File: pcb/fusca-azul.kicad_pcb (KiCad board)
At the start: 2 copper layers, 6 parts, among them J1 L298N Logic Jumpers, J2 HC-SR04, U1 ESP32-DEVKIT-V1

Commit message: feat: atualiza a pcb, mas falta corrigir tamanho e organização
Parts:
- removed J1: L298N Logic Jumpers, Connector_PinSocket_2.54mm:PinSocket_1x06_P2.54mm_Vertical
- removed J2: HC-SR04, Connector_PinSocket_2.54mm:PinSocket_1x04_P2.54mm_Vertical
- removed R1: 2k, Resistor_THT:R_Axial_DIN0207_L6.3mm_D2.5mm_P2.54mm_Vertical
- removed R2: 1k, Resistor_THT:R_Axial_DIN0207_L6.3mm_D2.5mm_P2.54mm_Vertical
- removed U1: ESP32-DEVKIT-V1, RF_Module:ESP32-C3-DevKitM-1
- added J3: HC-SR04, Connector_PinSocket_2.54mm:PinSocket_1x04_P2.54mm_Vertical, F.Cu at (150.7, 86.8)
- added J4: L298N Logic Jumpers, Connector_PinSocket_2.54mm:PinSocket_1x06_P2.54mm_Vertical, F.Cu at (112.0, 99.6)
- added J5: HC-SR04, Connector_PinSocket_2.54mm:PinSocket_1x04_P2.54mm_Vertical, F.Cu at (134.3, 60.6)
- added J6: HC-SR04, Connector_PinSocket_2.54mm:PinSocket_1x04_P2.54mm_Vertical, F.Cu at (107.7, 79.2)
- added R3: 2k, Resistor_THT:R_Axial_DIN0207_L6.3mm_D2.5mm_P2.54mm_Vertical, F.Cu at (145.3, 78.9)
- added R4: 1k, Resistor_THT:R_Axial_DIN0207_L6.3mm_D2.5mm_P2.54mm_Vertical, F.Cu at (145.3, 82.0)
- added R5: 2k, Resistor_THT:R_Axial_DIN0207_L6.3mm_D2.5mm_P2.54mm_Vertical, F.Cu at (126.1, 64.1)
- added R6: 1k, Resistor_THT:R_Axial_DIN0207_L6.3mm_D2.5mm_P2.54mm_Vertical, F.Cu at (129.3, 66.2)
- added R7: 2k, Resistor_THT:R_Axial_DIN0207_L6.3mm_D2.5mm_P2.54mm_Vertical, F.Cu at (111.2, 78.8)
- added R8: 1k, Resistor_THT:R_Axial_DIN0207_L6.3mm_D2.5mm_P2.54mm_Vertical, F.Cu at (113.6, 83.2)
- added U2: ESP32 - HW-394, fusca-azul:ESP32-HW-394, F.Cu at (118.8, 75.4)
- 5V_IN1: footprint TerminalBlock_Phoenix:TerminalBlock_Phoenix_PT-1,5-2-3.5-H_1x02_P3.50mm_Horizontal -> TerminalBlock_Phoenix:TerminalBlock_Phoenix_MKDS-1,5-2-5.08_1x02_P5.08mm_Horizontal
- moved 5V_IN1 47.3 mm to (108.1, 104.6)
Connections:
- 5V_IN1 pad 1: +5V -> GND
- 5V_IN1 pad 2: GND -> +5V
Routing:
- net GND: track 0.00 -> 167.8 mm, vias 0 -> 4
- net +5V: track 0.00 -> 143.8 mm
- net Net-(U2-D34): track 0.00 -> 29.7 mm
- net Net-(J5-Trig): track 0.00 -> 26.7 mm
- net Net-(J1-IN_3): track 19.9 -> 0.00 mm
- net Net-(J6-Trig): track 0.00 -> 16.2 mm
- net Net-(U2-D35): track 0.00 -> 11.6 mm
- net Net-(J3-Trig): track 0.00 -> 9.54 mm
- net Net-(J4-ENA): track 0.00 -> 9.40 mm
- net Net-(J4-IN_1): track 0.00 -> 8.35 mm
- net Net-(J4-IN_4): track 0.00 -> 8.35 mm
- net Net-(J4-IN_3): track 0.00 -> 8.35 mm
- net Net-(J4-IN_2): track 0.00 -> 8.35 mm
- net Net-(J4-ENB): track 0.00 -> 8.35 mm
- net Net-(J1-IN_2): track 7.50 -> 0.00 mm
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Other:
- board outline added: 56.5 x 65.2 mm

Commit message: feat: finaliza pcb
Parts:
- moved J5 55.1 mm to (86.5, 88.0), turned to 0 degrees
- moved J3 49.1 mm to (107.4, 110.0), turned to 90 degrees
- moved R6 44.6 mm to (91.5, 90.0), turned to -90 degrees
- moved R5 40.1 mm to (95.5, 90.0)
- moved 5V_IN1 38.0 mm to (87.0, 72.9)
- moved J6 32.2 mm to (135.5, 95.5), turned to 180 degrees
- moved J4 31.6 mm to (130.0, 73.7)
- moved U2 24.6 mm to (98.9, 60.9)
- moved R8 22.9 mm to (112.5, 106.0), turned to 90 degrees
- moved R7 21.2 mm to (112.5, 100.0)
- moved R4 15.4 mm to (130.0, 84.0)
- moved R3 15.4 mm to (130.0, 80.5)
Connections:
- J3 pad 2: Net-(J3-Trig) -> unconnected-(J3-Trig-Pad2)
- R3 pad 1: Net-(U2-D22) -> Net-(U2-RX2)
- R4 pad 1: Net-(U2-D22) -> Net-(U2-RX2)
- R4 pad 2: Net-(J3-Echo) -> Net-(J6-Echo)
- R5 pad 1: GND -> Net-(U2-D25)
- R5 pad 2: Net-(U2-D34) -> GND
- R6 pad 1: Net-(U2-D34) -> Net-(U2-D25)
- R7 pad 1: Net-(U2-D35) -> Net-(R7-Pad1)
- R8 pad 1: Net-(U2-D35) -> Net-(J3-Echo)
- R8 pad 2: Net-(J6-Echo) -> Net-(R7-Pad1)
- U2 pad 10: Net-(J6-Trig) -> unconnected-(U2-D32-Pad10)
- U2 pad 11: Net-(U2-D35) -> unconnected-(U2-D35-Pad11)
- U2 pad 12: Net-(U2-D34) -> unconnected-(U2-D34-Pad12)
- U2 pad 18: unconnected-(U2-D15-Pad18) -> Net-(J6-Trig)
- U2 pad 21: unconnected-(U2-RX2-Pad21) -> Net-(U2-RX2)
- U2 pad 22: unconnected-(U2-TX2-Pad22) -> Net-(J4-ENA)
- U2 pad 24: unconnected-(U2-D18-Pad24) -> Net-(J4-IN_1)
- U2 pad 25: unconnected-(U2-D19-Pad25) -> Net-(J4-IN_2)
- U2 pad 26: Net-(J3-Trig) -> Net-(J4-IN_3)
- U2 pad 29: Net-(U2-D22) -> Net-(J4-IN_4)
- U2 pad 3: Net-(J4-ENA) -> unconnected-(U2-D13-Pad3)
- U2 pad 30: Net-(J5-Trig) -> Net-(J4-ENB)
- U2 pad 5: Net-(J4-IN_1) -> unconnected-(U2-D14-Pad5)
- U2 pad 6: Net-(J4-IN_2) -> unconnected-(U2-D27-Pad6)
- U2 pad 7: Net-(J4-IN_3) -> unconnected-(U2-D26-Pad7)
- U2 pad 8: Net-(J4-IN_4) -> Net-(U2-D25)
- U2 pad 9: Net-(J4-ENB) -> Net-(J5-Trig)
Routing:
- net +5V: track 143.8 -> 96.8 mm
- net unconnected-(J3-Trig-Pad2): track 0.00 -> 30.8 mm
- net Net-(U2-D34): track 29.7 -> 0.00 mm
- net Net-(R7-Pad1): track 0.00 -> 27.9 mm
- net Net-(U2-D25): track 0.00 -> 16.8 mm
- net GND: track 167.8 -> 151.0 mm, vias 4 -> 2
- net Net-(U2-D35): track 11.6 -> 0.00 mm
- net Net-(J3-Trig): track 9.54 -> 0.00 mm
- net Net-(U2-RX2): track 0.00 -> 9.24 mm
- net Net-(J5-Trig): track 26.7 -> 19.5 mm
- net Net-(U2-D22): track 7.08 -> 0.00 mm
- net Net-(J6-Trig): track 16.2 -> 11.8 mm
- net Net-(J6-Echo): track 3.84 -> 7.66 mm
- net Net-(J4-IN_4): track 8.35 -> 5.71 mm
- net Net-(J4-ENB): track 8.35 -> 5.71 mm
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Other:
- board size 56.5 x 65.2 mm -> 59 x 67.5 mm

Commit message: fix: corrige ligacao na placa
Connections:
- J3 pad 2: unconnected-(J3-Trig-Pad2) -> Net-(J3-Trig)
- R7 pad 1: Net-(R7-Pad1) -> Net-(U2-D26)
- R8 pad 2: Net-(R7-Pad1) -> Net-(U2-D26)
- U2 pad 6: unconnected-(U2-D27-Pad6) -> Net-(J3-Trig)
- U2 pad 7: unconnected-(U2-D26-Pad7) -> Net-(U2-D26)
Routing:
- net unconnected-(J3-Trig-Pad2): track 30.8 -> 0.00 mm
- net Net-(J3-Trig): track 0.00 -> 30.8 mm
- net GND: track 151.0 -> 179.1 mm, vias 2 -> 0
- net Net-(U2-D26): track 0.00 -> 27.9 mm
- net Net-(R7-Pad1): track 27.9 -> 0.00 mm
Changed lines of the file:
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@@
 			(at 0 -2.77 0)
 			(layer "F.SilkS")
+			(hide yes)
 			(effects
 				(font
@@
 			(at 0 -2.77 0)
 			(layer "F.SilkS")
+			(hide yes)
 			(effects
 				(font
@@
 			(at 1.27 -2.37 90)
 			(layer "F.SilkS")
+			(hide yes)
 			(effects
 				(font
@@
 			(at 0 -2.77 0)
 			(layer "F.SilkS")
+			(hide yes)
 			(effects
 				(font
@@
 			(at 0 -2.77 90)
 			(layer "F.SilkS")
+			(hide yes)
 			(effects
 				(font
@@
 			(layers "*.Cu" "*.Mask")
 			(remove_unused_layers no)
-			(net "unconnected-(J3-Trig-Pad2)")
+			(net "Net-(J3-Trig)")
 			(pinfunction "Trig_2")
 			(pintype "input")
@@
 			(keep_end_layers yes)
 			(zone_layer_connections)
-			(net "unconnected-(U2-D27-Pad6)")
+			(net "Net-(J3-Trig)")
 			(pinfunction "D27_6")
 			(pintype "bidirectional")
@@
 			(keep_end_layers yes)
 			(zone_layer_connections)
-			(net "unconnected-(U2-D26-Pad7)")
+			(net "Net-(U2-D26)")
 			(pinfunction "D26_7")
 			(pintype "bidirectional")
@@
 			(at 1.27 -2.37 90)
 			(layer "F.SilkS")
+			(hide yes)
 			(effects
 				(font
@@
 			(at 1.27 -2.37 0)
 			(layer "F.SilkS")
+			(hide yes)
 			(effects
 				(font
@@
 			(at 1.27 -2.37 0)
 			(layer "F.SilkS")
+			(hide yes)
 			(effects
 				(font
@@
 			(layers "*.Cu" "*.Mask")
 			(remove_unused_layers no)
-			(net "Net-(R7-Pad1)")
+			(net "Net-(U2-D26)")
 			(pintype "passive")
 		)
@@
 			(at 1.27 -2.37 90)
 			(layer "F.SilkS")
+			(hide yes)
 			(effects
 				(font
@@
 			(layers "*.Cu" "*.Mask")
 			(remove_unused_layers no)
-			(net "Net-(R7-Pad1)")
+			(net "Net-(U2-D26)")
 			(pintype "passive")
 		)
@@
 			(at 1.27 -2.37 0)
 			(layer "F.SilkS")
+			(hide yes)
 			(effects
 				(font
@@
 	)
 	(segment
-		(start 115.04 110)
-		(end 115.04 100.04)
+		(start 121 51)
+		(end 121 97)
 		(width 1)
 		(layer "F.Cu")
@@
 	)
 	(segment
-		(start 129.605 93.895)
-		(end 130 93.5)
+		(start 115.04 110)
+		(end 115.04 100.04)
 		(width 1)
 		(layer "F.Cu")
@@
 	)
 	(segment
-		(start 124.325 93.895)
-		(end 129.605 93.895)
+		(start 92.46 95.58)
+		(end 95.5 92.54)
 		(width 1)
 		(layer "F.Cu")
@@
 	)
 	(segment
-		(start 92.46 95.58)
-		(end 95.5 92.54)
+		(start 121 51)
+		(end 122 51)
 		(width 1)
 		(layer "F.Cu")
@@
 	)
 	(segment
-		(start 118.22 100)
+		(start 121.11 97.11)
 		(end 122.11 96.11)
 		(width 1)
@@
 	(segment
 		(start 98.5 51)
-		(end 122 51)
+		(end 121 51)
 		(width 1)
 		(layer "F.Cu")
@@
 	)
 	(segment
+		(start 118.22 100)
+		(end 121.11 97.11)
+		(width 1)
+		(layer "F.Cu")
+		(net "GND")
+	)
+	(segment
 		(start 95.5 54)
 		(end 98.5 51)
@@
 		(net "GND")
 	)
-	(via
-		(at 135.5 83.505)
-		(size 0.6)
-		(drill 0.3)
-		(layers "F.Cu" "B.Cu")
-		(net "GND")
-	)
-	(via
-		(at 130 93.5)
-		(size 0.6)
-		(drill 0.3)
-		(layers "F.Cu" "B.Cu")
-		(net "GND")
-	)
 	(segment
-		(start 130 93.5)
-		(end 130 89.005)
+		(start 121 97)
+		(end 121.11 97.11)
 		(width 1)
-		(layer "B.Cu")
-		(net "GND")
-	)
-	(segment
-		(start 130 89.005)
-		(end 135.5 83.505)
-		(width 1)
-		(layer "B.Cu")
+		(layer "F.Cu")
 		(net "GND")
 	)
@@
 		(width 0.5)
 		(layer "F.Cu")
-		(net "unconnected-(J3-Trig-Pad2)")
+		(net "Net-(J3-Trig)")
 	)
 	(segment
@@
 		(width 0.5)
 		(layer "F.Cu")
-		(net "unconnected-(J3-Trig-Pad2)")
+		(net "Net-(J3-Trig)")
 	)
 	(segment
@@
 		(width 0.5)
 		(layer "F.Cu")
-		(net "Net-(R7-Pad1)")
+		(net "Net-(U2-D26)")
 	)
 	(segment
@@
 		(width 0.5)
 		(layer "F.Cu")
-		(net "Net-(R7-Pad1)")
+		(net "Net-(U2-D26)")
 	)
 	(segment
@@
 		(width 0.5)
 		(layer "F.Cu")
-		(net "Net-(R7-Pad1)")
+		(net "Net-(U2-D26)")
 	)
 	(segment
@@
 		(width 0.5)
 		(layer "F.Cu")
-		(net "Net-(R7-Pad1)")
+		(net "Net-(U2-D26)")
 	)
 	(embedded_fonts no)

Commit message: finaliza pcb
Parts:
- removed J6: HC-SR04, Connector_PinSocket_2.54mm:PinSocket_1x04_P2.54mm_Vertical
- removed R3: 2k, Resistor_THT:R_Axial_DIN0207_L6.3mm_D2.5mm_P2.54mm_Vertical
- removed R4: 1k, Resistor_THT:R_Axial_DIN0207_L6.3mm_D2.5mm_P2.54mm_Vertical
- R5, R6, R7, R8: footprint Resistor_THT:R_Axial_DIN0207_L6.3mm_D2.5mm_P2.54mm_Vertical -> Resistor_THT:R_Axial_DIN0207_L6.3mm_D2.5mm_P5.08mm_Vertical
- moved 5V_IN1 83.3 mm to (154.0, 122.4), turned to 90 degrees
- moved R5 37.2 mm to (111.6, 123.5)
- moved U2 34.2 mm to (119.7, 88.0)
- moved R6 33.6 mm to (106.7, 119.9), turned to 0 degrees
- moved J5 32.3 mm to (102.8, 115.9)
- moved J4 30.2 mm to (152.3, 94.0), turned to 0 degrees
- moved J3 27.9 mm to (102.9, 82.5), turned to 0 degrees
- moved R8 18.9 mm to (107.7, 87.8), turned to 0 degrees
- moved R7 9.53 mm to (107.8, 91.7)
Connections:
- R5 pad 1: Net-(U2-D25) -> Net-(U2-D14)
- R6 pad 1: Net-(U2-D25) -> Net-(J5-Echo)
- R6 pad 2: Net-(J5-Echo) -> Net-(U2-D14)
- R7 pad 1: Net-(U2-D26) -> GND
- R7 pad 2: GND -> Net-(U2-D26)
- U2 pad 18: Net-(J6-Trig) -> unconnected-(U2-D15-Pad18)
- U2 pad 20: unconnected-(U2-D4-Pad20) -> Net-(J4-ENB)
- U2 pad 21: Net-(U2-RX2) -> unconnected-(U2-RX2-Pad21)
- U2 pad 22: Net-(J4-ENA) -> unconnected-(U2-TX2-Pad22)
- U2 pad 24: Net-(J4-IN_1) -> Net-(J4-IN_4)
- U2 pad 25: Net-(J4-IN_2) -> Net-(J4-IN_3)
- U2 pad 26: Net-(J4-IN_3) -> Net-(J4-IN_2)
- U2 pad 29: Net-(J4-IN_4) -> Net-(J4-IN_1)
- U2 pad 30: Net-(J4-ENB) -> Net-(J4-ENA)
- U2 pad 5: unconnected-(U2-D14-Pad5) -> Net-(U2-D14)
- U2 pad 6: Net-(J3-Trig) -> Net-(J5-Trig)
- U2 pad 8: Net-(U2-D25) -> unconnected-(U2-D25-Pad8)
- U2 pad 9: Net-(J5-Trig) -> Net-(J3-Trig)
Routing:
- net GND: track 179.1 -> 131.0 mm
- net +5V: track 96.8 -> 143.8 mm
- net Net-(U2-D25): track 16.8 -> 0.00 mm
- net Net-(U2-D14): track 0.00 -> 14.3 mm
- net Net-(J6-Trig): track 11.8 -> 0.00 mm
- net Net-(U2-RX2): track 9.24 -> 0.00 mm
- net Net-(J6-Echo): track 7.66 -> 0.00 mm
- net Net-(U2-D26): track 27.9 -> 23.4 mm
- net Net-(J4-ENB): track 5.71 -> 9.96 mm
- net Net-(J4-IN_1): track 7.74 -> 9.65 mm
- net Net-(J4-IN_4): track 5.71 -> 7.55 mm
- net Net-(J3-Trig): track 30.8 -> 32.7 mm
- net Net-(J3-Echo): track 3.96 -> 4.88 mm
- net Net-(J5-Echo): track 5.23 -> 4.32 mm
- net Net-(J5-Trig): track 19.5 -> 20.1 mm
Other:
- board size 59 x 67.5 mm -> 64.6 x 55.3 mm

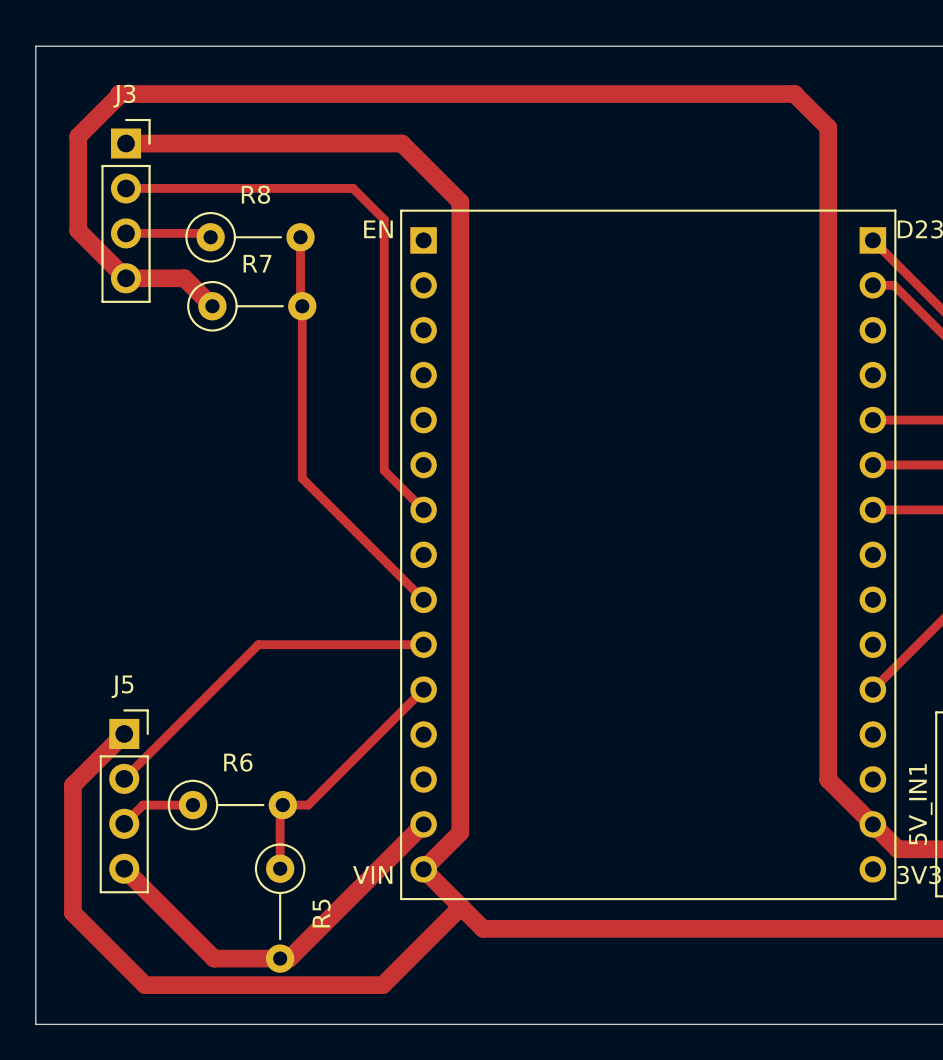
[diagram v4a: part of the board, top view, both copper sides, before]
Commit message: corrige pcb com espaçamento erraado
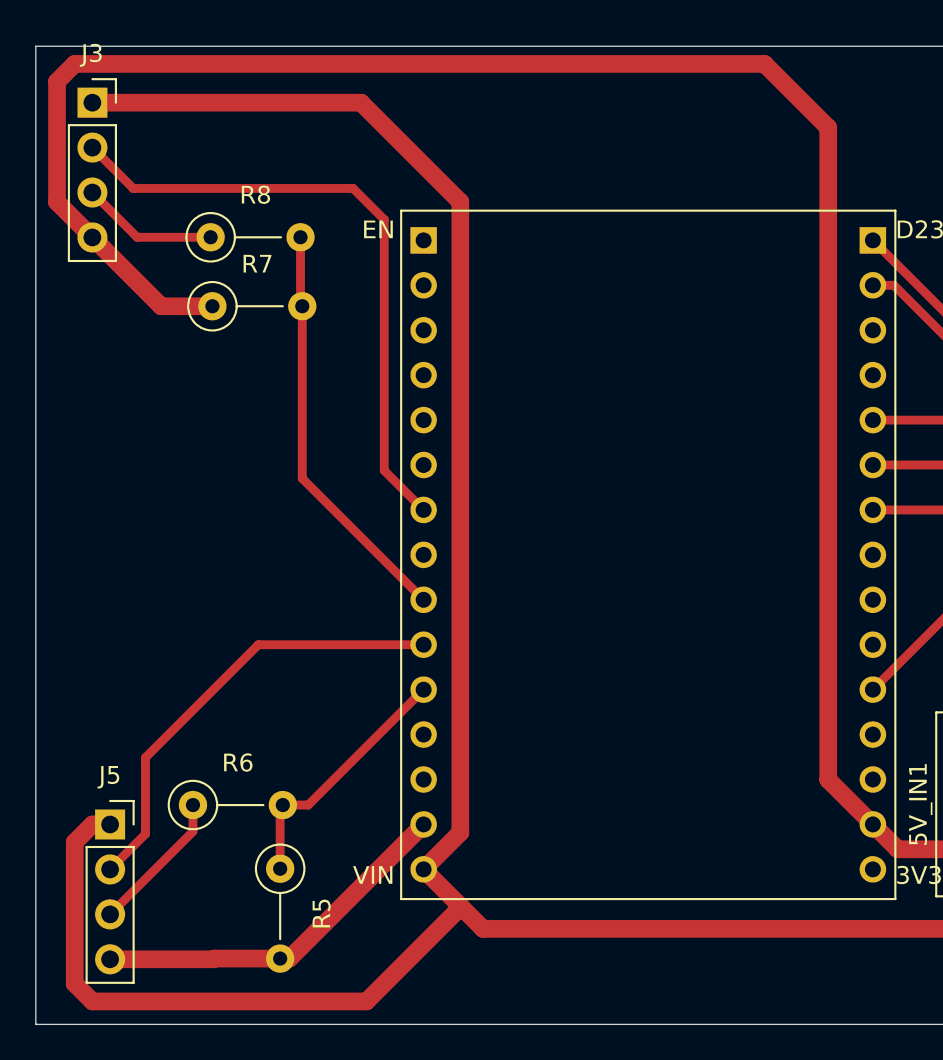
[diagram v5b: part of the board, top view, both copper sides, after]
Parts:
- moved J5 5.18 mm to (102.0, 121.0)
- moved J3 2.99 mm to (101.0, 80.2)
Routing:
- net Net-(J5-Trig): track 20.1 -> 25.5 mm
- net Net-(J5-Echo): track 4.32 -> 8.12 mm
- net GND: track 131.0 -> 134.3 mm
- net Net-(J3-Echo): track 4.88 -> 8.04 mm
- net Net-(J3-Trig): track 32.7 -> 35.5 mm
- net +5V: track 143.8 -> 144.7 mm
